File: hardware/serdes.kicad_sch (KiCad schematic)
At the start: 22 parts, among them Q3 BSS138, U4 CCGM1A1, X2 100 MHz LVDS 3.2x2.5

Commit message: Adding USB connector and level converter
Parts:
- U4: footprint Package_BGA:BGA-324_15.0x15.0mm_Layout18x18_P0.8mm_Ball0.45mm_Pad0.4mm_NSMD -> ulx5m-gs:BGA-324_15.0x15.0mm_Layout18x18_P0.8mm_Ball0.45mm_Pad0.4mm_NSMD
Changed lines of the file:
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@@
 			)
 		)
-		(property "Footprint" "Package_BGA:BGA-324_15.0x15.0mm_Layout18x18_P0.8mm_Ball0.45mm_Pad0.4mm_NSMD"
+		(property "Footprint" "ulx5m-gs:BGA-324_15.0x15.0mm_Layout18x18_P0.8mm_Ball0.45mm_Pad0.4mm_NSMD"
 			(at 143.51 96.52 0)
 			(effects
@@
 			)
 		)
-		(property "Footprint" "Package_BGA:BGA-324_15.0x15.0mm_Layout18x18_P0.8mm_Ball0.45mm_Pad0.4mm_NSMD"
+		(property "Footprint" "ulx5m-gs:BGA-324_15.0x15.0mm_Layout18x18_P0.8mm_Ball0.45mm_Pad0.4mm_NSMD"
 			(at 143.51 34.29 0)
 			(effects

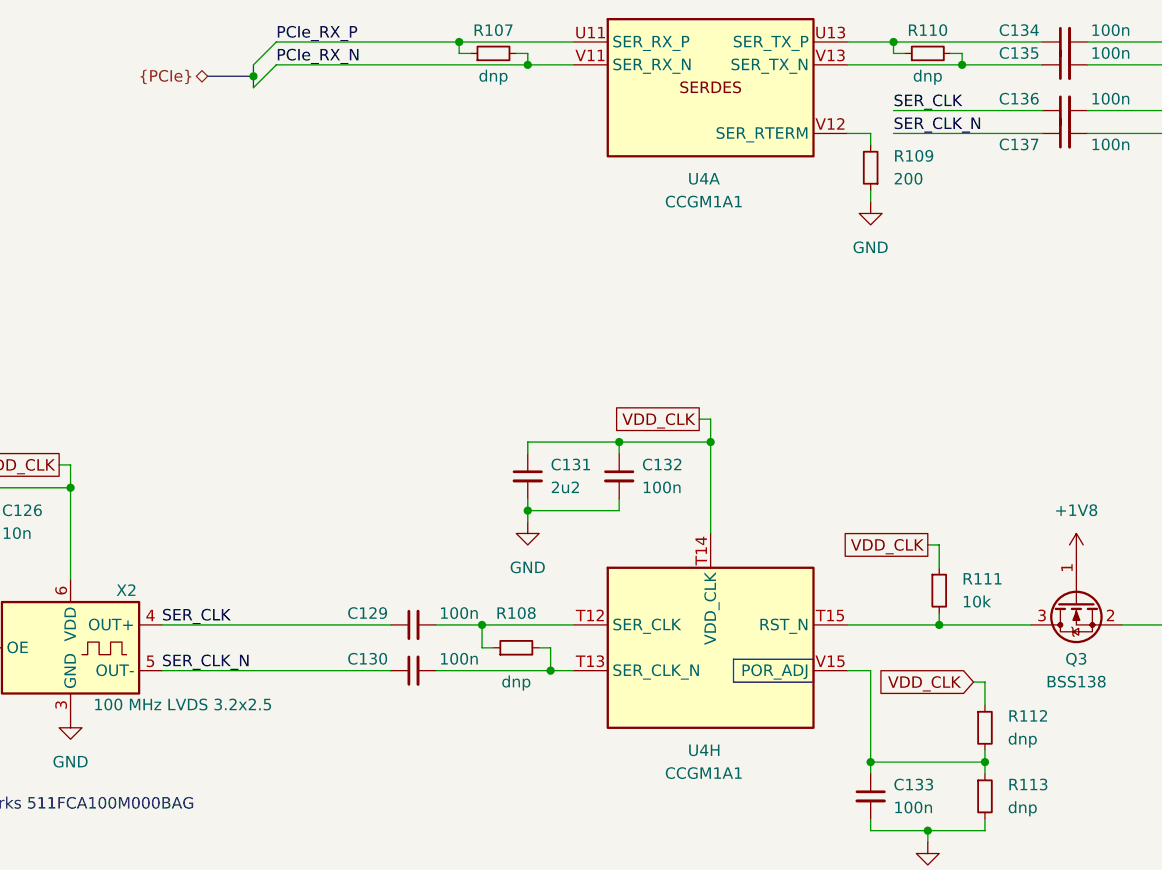
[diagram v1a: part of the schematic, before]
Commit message: Routing diff clock
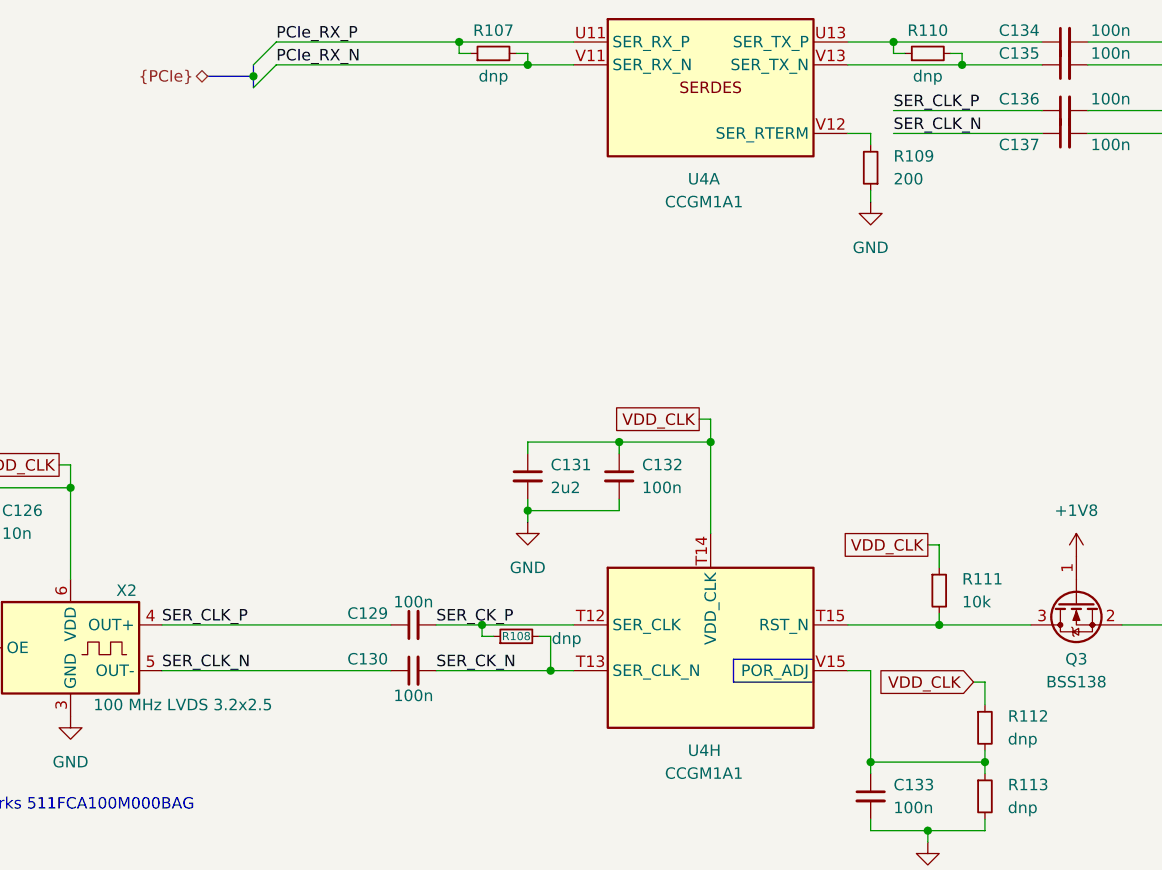
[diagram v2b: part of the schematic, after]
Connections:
- net SER_CK_P: now reaches C129.2, R108.1, U4.T12 (SER_CLK)
- net SER_CK_N: now reaches C130.2, R108.2, U4.T13 (SER_CLK_N)
- net SER_CLK renamed SER_CLK_P
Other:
- company: (none) -> ${project_creator}
- title: (none) -> ${project_name}
- moved on the sheet: R108
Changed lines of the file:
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@@
 	(generator_version "9.0")
 	(paper "A4")
+	(title_block
+		(title "${project_name}")
+		(date "2025-06-24")
+		(rev "${project_version}")
+		(company "${project_creator}")
+		(comment 1 "${project_license}")
+	)
 	(rectangle
 		(start 151.13 114.3)
@@
 	(wire
 		(pts
-			(xy 130.81 113.03) (xy 130.81 115.57)
+			(xy 130.81 111.76) (xy 130.81 115.57)
 		)
 		(stroke
@@
 	(wire
 		(pts
-			(xy 123.19 110.49) (xy 123.19 113.03)
+			(xy 123.19 110.49) (xy 123.19 111.76)
 		)
 		(stroke
@@
 	(wire
 		(pts
-			(xy 124.46 113.03) (xy 123.19 113.03)
+			(xy 124.46 111.76) (xy 123.19 111.76)
 		)
 		(stroke
@@
 	(wire
 		(pts
-			(xy 129.54 113.03) (xy 130.81 113.03)
+			(xy 129.54 111.76) (xy 130.81 111.76)
 		)
 		(stroke
@@
 		)
 	)
+	(label "SER_CK_P"
+		(at 118.11 110.49 0)
+		(effects
+			(font
+				(size 1.27 1.27)
+			)
+			(justify left bottom)
+		)
+	)
 	(label "PCIe_CLK_N"
 		(at 210.82 55.88 180)
@@
 		)
 	)
-	(label "SER_CLK"
+	(label "SER_CLK_P"
 		(at 168.91 53.34 0)
 		(effects
@@
 		)
 	)
-	(label "SER_CLK"
+	(label "SER_CK_N"
+		(at 118.11 115.57 0)
+		(effects
+			(font
+				(size 1.27 1.27)
+			)
+			(justify left bottom)
+		)
+	)
+	(label "SER_CLK_P"
 		(at 87.63 110.49 0)
 		(effects
@@
 		)
 		(property "Value" "100n"
-			(at 120.65 109.22 90)
+			(at 115.57 107.95 90)
 			(effects
 				(font
@@
 		(lib_name "R_Small_1")
 		(lib_id "Device:R_Small")
-		(at 127 113.03 90)
+		(at 127 111.76 90)
 		(unit 1)
 		(exclude_from_sim no)
@@
 		(dnp no)
 		(property "Reference" "R108"
-			(at 127 109.22 90)
+			(at 127 111.76 90)
 			(effects
 				(font
-					(size 1.27 1.27)
+					(size 0.9 0.9)
 				)
 			)
 		)
 		(property "Value" "dnp"
-			(at 127 116.84 90)
+			(at 132.588 112.014 90)
 			(effects
 				(font
@@
 		)
 		(property "Footprint" "Resistor_SMD:R_0402_1005Metric"
-			(at 127 113.03 0)
+			(at 127 111.76 0)
 			(effects
 				(font
@@
 		)
 		(property "Datasheet" "~"
-			(at 127 113.03 0)
+			(at 127 111.76 0)
 			(effects
 				(font
@@
 		)
 		(property "Description" ""
-			(at 127 113.03 0)
+			(at 127 111.76 0)
 			(effects
 				(font
@@
 		)
 		(property "Value" "100n"
-			(at 120.65 114.3 90)
+			(at 115.57 118.364 90)
 			(effects
 				(font

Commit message: routing PCIe
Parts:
- R110: now not fitted
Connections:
- net PCIe_TX_BC_P: now reaches C134.1, R110.1, U4.U13 (SER_TX_P)
- net PCIe_TX_BC_N: now reaches C135.1, R110.2, U4.V13 (SER_TX_N)
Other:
- moved on the sheet: C134, C135, C136, C137

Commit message: Routing
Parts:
- Q3: footprint Package_TO_SOT_SMD:SOT-23 -> Package_TO_SOT_SMD:SOT-523
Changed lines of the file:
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@@
 			)
 		)
-		(property "Footprint" "Package_TO_SOT_SMD:SOT-23"
+		(property "Footprint" "Package_TO_SOT_SMD:SOT-523"
 			(at 191.135 113.03 0)
 			(effects

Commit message: Cleanup
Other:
- moved on the sheet: C126, C129, C130, C131, C132, C133, C134, C135, C136, C137, C138, Q3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

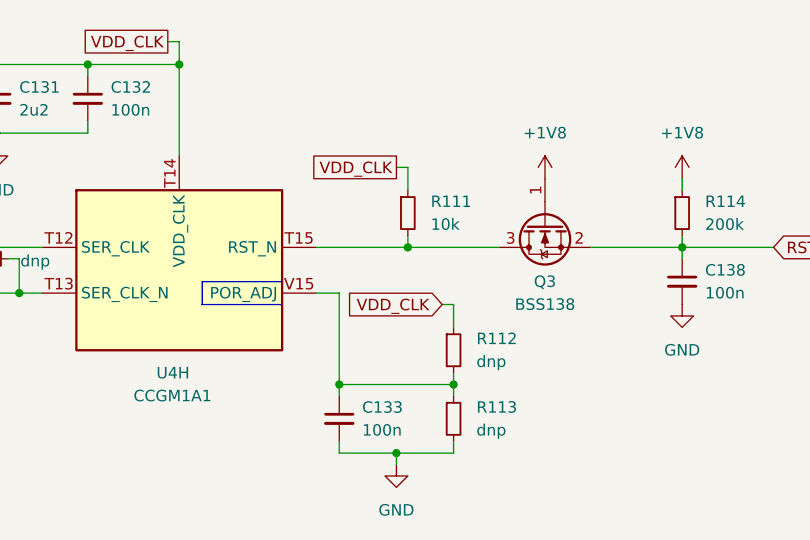
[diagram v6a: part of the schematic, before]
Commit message: GPIO are now routed differential
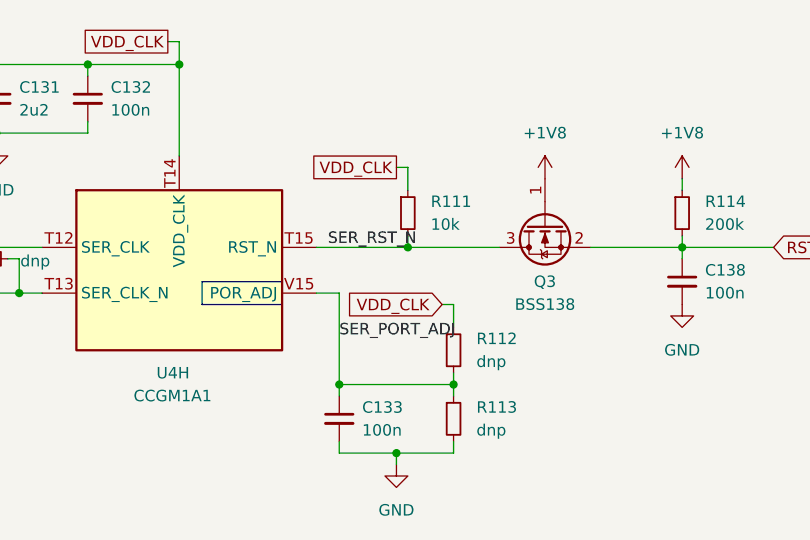
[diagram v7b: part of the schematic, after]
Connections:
- net SER_RST_N: now reaches Q3.3 (D), R111.2, U4.T15 (RST_N)
- net SER_PORT_ADJ: now reaches C133.1, R112.2, R113.1, U4.V15 (POR_ADJ)
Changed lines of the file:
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@@
+		)
+	)
+	(label "SER_RST_N"
+		(at 125.73 86.36 0)
+		(effects
+			(font
+				(size 1.27 1.27)
+			)
+			(justify left bottom)
 		)
 	)
@@
 		(effects
 			(font
+				(size 1.27 1.27)
+			)
+			(justify left bottom)
+		)
+	)
+	(label "SER_PORT_ADJ"
+		(at 127 96.52 0)
+		(effects
+			(font

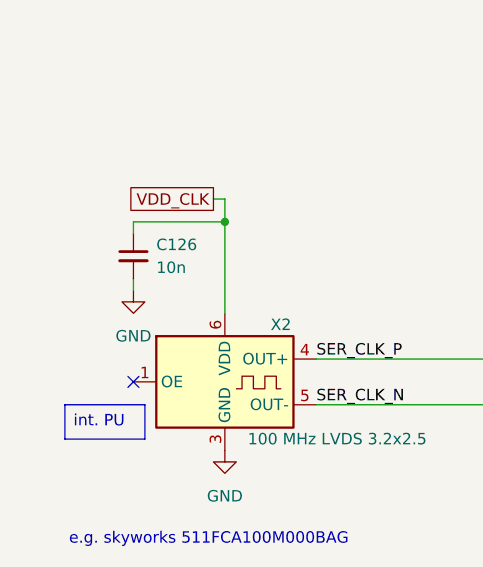
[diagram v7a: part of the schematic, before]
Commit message: Adding PullUP to OE on SerDes CLK - also moved so it can be placed
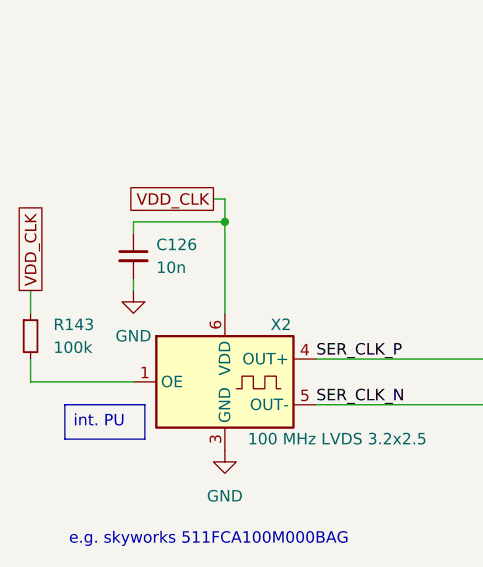
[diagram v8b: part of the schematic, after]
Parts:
- added R143: 100k, Resistor_SMD:R_0402_1005Metric, symbol Device:R_Small
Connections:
- net VDD_CLK: now also R143.1
- net at X2.1 (OE): now also R143.2
- no-connect marks 1 -> 0
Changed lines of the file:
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@@
 		(color 0 0 0 0)
 	)
-	(no_connect
-		(at 27.94 88.9)
-	)
 	(bus_entry
 		(at 171.45 31.75)
@@
 	(wire
 		(pts
+			(xy 16.51 78.74) (xy 16.51 81.28)
+		)
+		(stroke
+			(width 0)
+			(type default)
+		)
+	)
+	(wire
+		(pts
 			(xy 127 101.6) (xy 139.7 101.6)
 		)
@@
 	(wire
 		(pts
+			(xy 16.51 88.9) (xy 27.94 88.9)
+		)
+		(stroke
+			(width 0)
+			(type default)
+		)
+	)
+	(wire
+		(pts
 			(xy 151.13 39.37) (xy 171.45 39.37)
 		)
@@
 		)
 	)
+	(wire
+		(pts
+			(xy 16.51 86.36) (xy 16.51 88.9)
+		)
+		(stroke
+			(width 0)
+			(type default)
+		)
+	)
 	(bus
 		(pts
@@
 		)
 	)
+	(global_label "VDD_CLK"
+		(shape passive)
+		(at 16.51 78.74 90)
+		(fields_autoplaced yes)
+		(effects
+			(font
+				(size 1.27 1.27)
+			)
+			(justify left)
+		)
+		(property "Intersheetrefs" "${INTERSHEET_REFS}"
+			(at 16.51 68.7018 90)
+			(effects
+				(font
+					(size 1.27 1.27)
+				)
+				(justify left)
+				(hide yes)
+			)
+		)
+	)
 	(hierarchical_label "{PCIe}"
 		(shape bidirectional)
@@
 					(unit 1)
 				)
+			)
+		)
+	)
+	(symbol
+		(lib_id "Device:R_Small")
+		(at 16.51 83.82 0)
+		(unit 1)
+		(exclude_from_sim no)
+		(in_bom yes)
+		(on_board yes)
+		(dnp no)
+		(fields_autoplaced yes)
+		(property "Reference" "R143"
+			(at 19.05 82.5499 0)
+			(effects
+				(font
+					(size 1.27 1.27)
+				)
+				(justify left)
+			)
+		)
+		(property "Value" "100k"
+			(at 19.05 85.0899 0)
+			(effects
+				(font
+					(size 1.27 1.27)
+				)
+				(justify left)
+			)
+		)
+		(property "Footprint" "Resistor_SMD:R_0402_1005Metric"
+			(at 16.51 83.82 0)
+			(effects
+				(font
+					(size 1.27 1.27)
+				)
+				(hide yes)
+			)
+		)
+		(property "Datasheet" "~"
+			(at 16.51 83.82 0)
+			(effects
+				(font
+					(size 1.27 1.27)
+				)
+				(hide yes)
+			)
+		)
+		(property "Description" "Resistor, small symbol"
+			(at 16.51 83.82 0)
+			(effects
+				(font
+					(size 1.27 1.27)
+				)
+				(hide yes)
+			)
+		)
+		(pin "2"
+		)
+		(pin "1"
+		)
+		(instances
+			(project "ulx5m-gs"
+				(path "/9e5cbfd6-8186-4817-919e-acd256336bc8/1df60d8c-4085-48d0-b19e-6bdaeb1198b0"
+					(reference "R143")
+					(unit 1)
+				)
